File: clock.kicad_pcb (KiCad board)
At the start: 2 copper layers, 133 parts, among them J1 USB_C_Receptacle_USB2.0_16P, J3 Conn_01x02_Pin, J4 Conn_01x02_Pin, J5 Battery, Q1 2N7002K, Q2 NPN, SW1 SW_SPST, SW2 SW_SPST, SW5 SW_SPST, U1 STM32F072CBT6, U2 USBLC6-2SC6, U4 MCP73871-2CC, U5 AP2112K-3.3, Y1 8MHz

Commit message: am I ok??? is this too close. Nearly done!! mabye..
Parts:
- added C15: 10uF, Capacitor_SMD:C_0603_1608Metric_Pad1.08x0.95mm_HandSolder, F.Cu at (216.0, 38.5)
- added D1: D_Small, Diode_SMD:D_SOD-123F, F.Cu at (252.6, 59.6)
- added SW4: SW_SPDT, FB_clock_lib:SW_slide, B.Cu at (253.8, 44.0)
- D74, Q1, R12: moved to F.Cu
- moved BZ1 78.9 mm to (250.4, 58.8), turned to -90 degrees
- moved Q2 78.1 mm to (252.4, 51.0), turned to 0 degrees
- moved R13 75.5 mm to (249.8, 48.0), turned to -90 degrees
- moved Q1 61.1 mm to (227.3, 30.1)
- moved R12 60.9 mm to (230.8, 31.0), turned to 0 degrees
- moved R14 60.9 mm to (250.2, 42.0), turned to 90 degrees
- moved R15 59.9 mm to (249.0, 40.6), turned to -90 degrees
- moved R31 59.9 mm to (249.6, 44.9), turned to 90 degrees
- moved D74 58.9 mm to (248.1, 44.3), turned to 90 degrees
- moved R7 57.9 mm to (226.0, 33.6), turned to 180 degrees
- moved SW5 34.1 mm to (221.2, 61.6), turned to 0 degrees
- moved SW1 26.6 mm to (230.2, 61.6), turned to 0 degrees
- moved SW2 21.2 mm to (239.6, 61.6), turned to 0 degrees
- moved C7 1.61 mm to (252.6, 38.0), turned to 0 degrees
- moved C8 0.70 mm to (249.8, 37.4)
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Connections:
- U1 pad 10: unconnected-(U1-PA0-Pad10) -> 5V_TEST
- U1 pad 11: unconnected-(U1-PA1-Pad11) -> BUZZER
- U1 pad 39: LBO -> CE
- U1 pad 40: unconnected-(U1-PB4-Pad40) -> LBO
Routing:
- net GND: track 114.8 -> 156.4 mm, vias 15 -> 14
- net +5V: track 28.7 -> 65.9 mm, vias 4 -> 7
- net +3.3V: track 78.3 -> 107.2 mm, vias 2 -> 5
- net BUZZER: track 0.00 -> 13.8 mm
- net CE: track 0.00 -> 11.7 mm, vias 0 -> 1
- net 5V_TEST: track 0.00 -> 9.68 mm, vias 0 -> 2
- net Net-(BZ1--): track 0.00 -> 8.93 mm, vias 0 -> 1
- net Net-(Q1-D): track 0.00 -> 7.51 mm, vias 0 -> 1
- net Net-(SW4-B): track 0.00 -> 5.32 mm
- net M5: track 97.5 -> 94.9 mm
- net Net-(Q1-G): track 0.00 -> 2.00 mm
- net Net-(Q2-B): track 0.00 -> 1.89 mm
- net Net-(D74-A): track 0.00 -> 1.83 mm, vias 0 -> 1
- net LBO: track 33.4 -> 34.4 mm
- net M3: track 88.2 -> 87.4 mm
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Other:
- board outline added: 51.4 x 38.8 mm

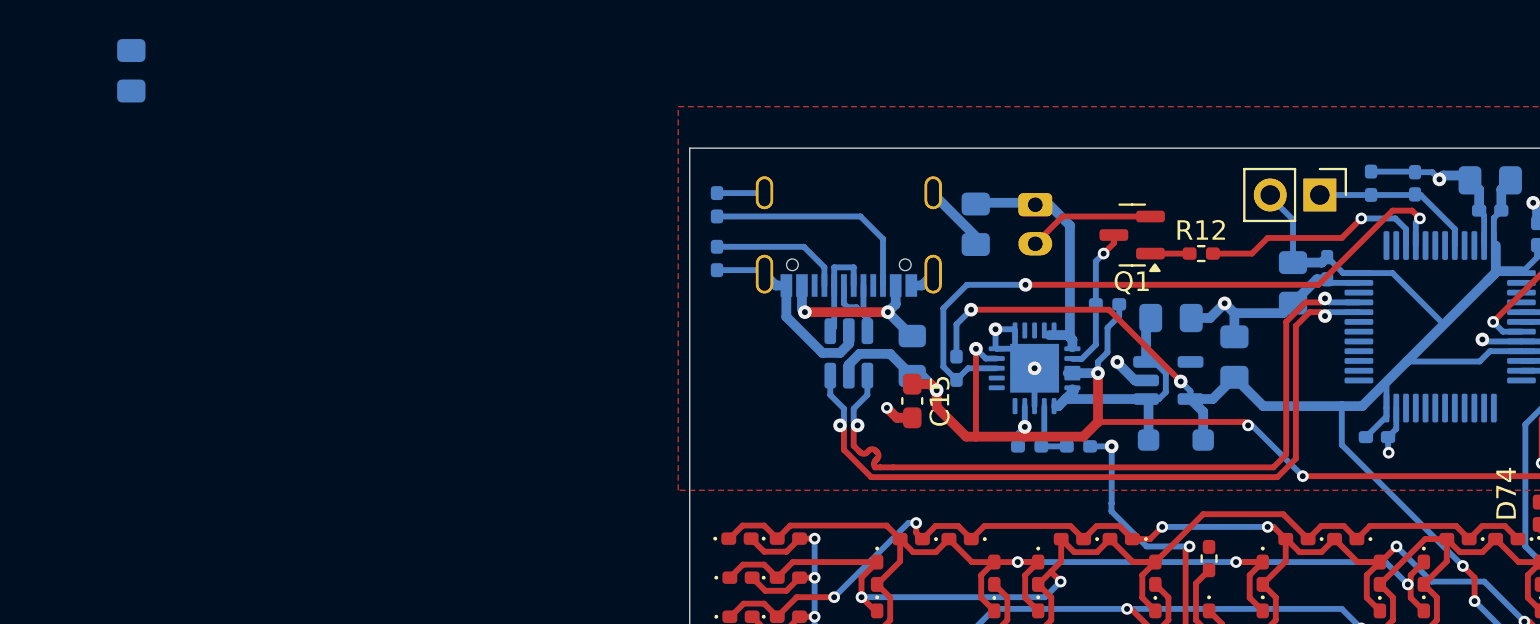
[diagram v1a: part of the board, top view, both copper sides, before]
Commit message: fixed weird kicad bug, added last few components, just need to add charlie plexed resistors + wire it up
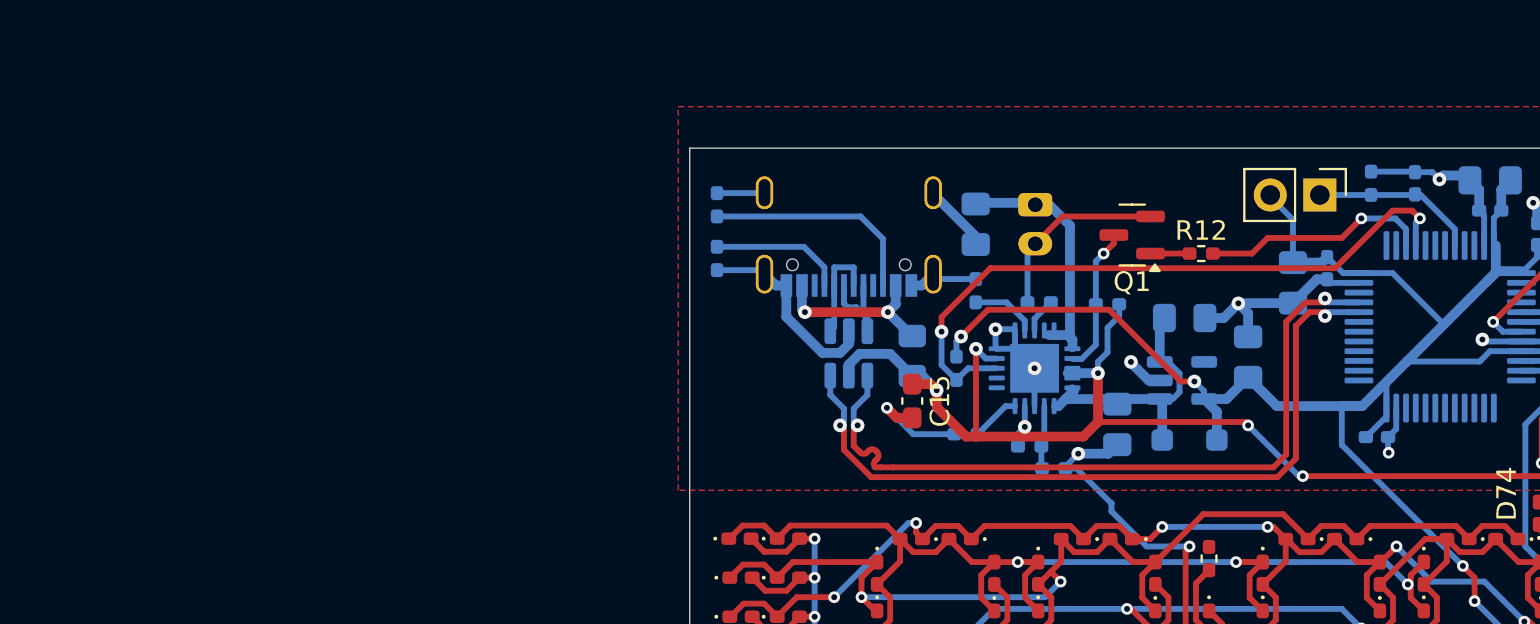
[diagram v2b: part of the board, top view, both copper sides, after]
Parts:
- added R5: 2k, Resistor_SMD:R_0402_1005Metric_Pad0.72x0.64mm_HandSolder, B.Cu at (222.5, 33.5)
- added R8: 100k, Resistor_SMD:R_0402_1005Metric_Pad0.72x0.64mm_HandSolder, B.Cu at (219.2, 32.9)
- added R9: 10k, Resistor_SMD:R_0402_1005Metric_Pad0.72x0.64mm_HandSolder, B.Cu at (218.8, 40.2)
- moved C16 53.6 mm to (226.5, 39.8), turned to 90 degrees
- moved R11 1.69 mm to (223.2, 42.0)
- moved C18 0.70 mm to (229.9, 34.3)
- moved C19 0.70 mm to (233.2, 36.3)
- moved D76 0.70 mm to (230.2, 40.5)
- moved U5 0.70 mm to (229.8, 37.5)
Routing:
- net GND: track 156.4 -> 167.9 mm
- net Net-(U4-PROG3): track 0.00 -> 3.40 mm
- net Net-(U4-THERM): track 0.00 -> 2.51 mm
- net Net-(U4-PROG1): track 0.00 -> 1.78 mm
- net VCC: track 13.3 -> 14.0 mm

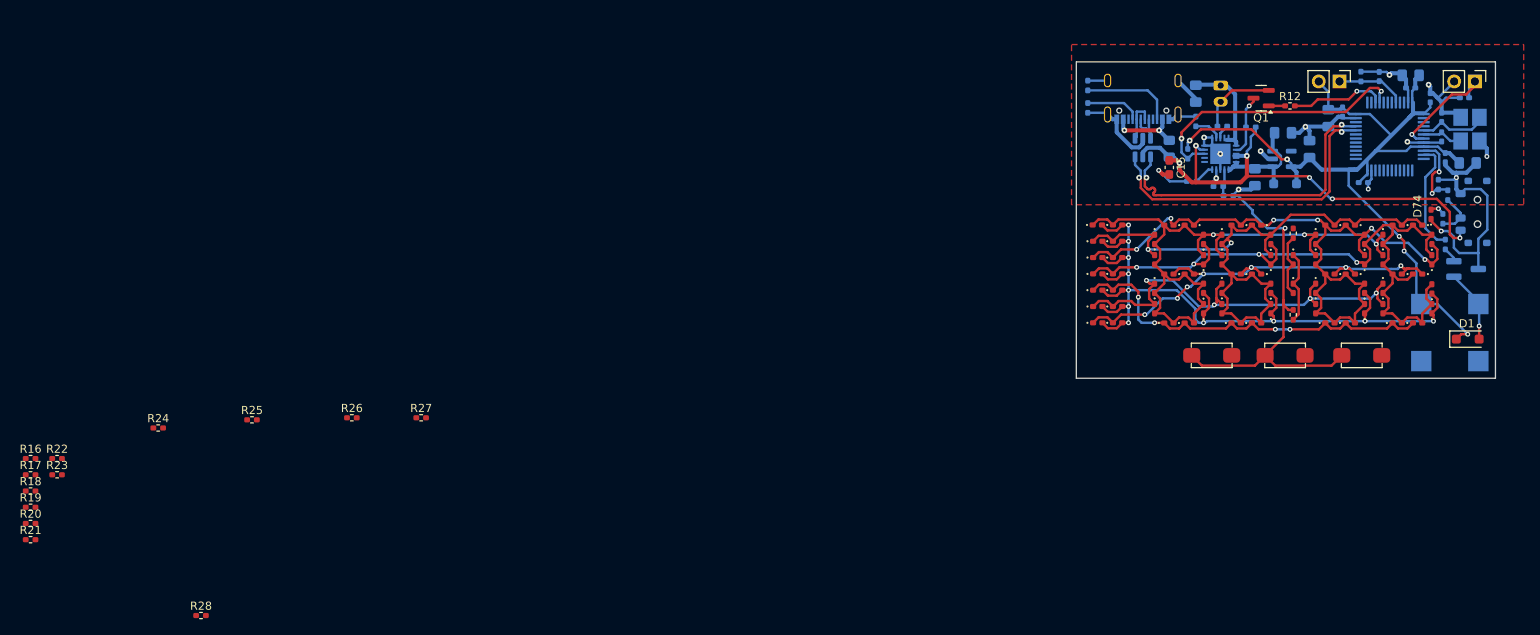
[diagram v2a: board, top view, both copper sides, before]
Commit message: all wiring done, need to clean up silk screen edge clips + double check pins for charlieplex & buttons
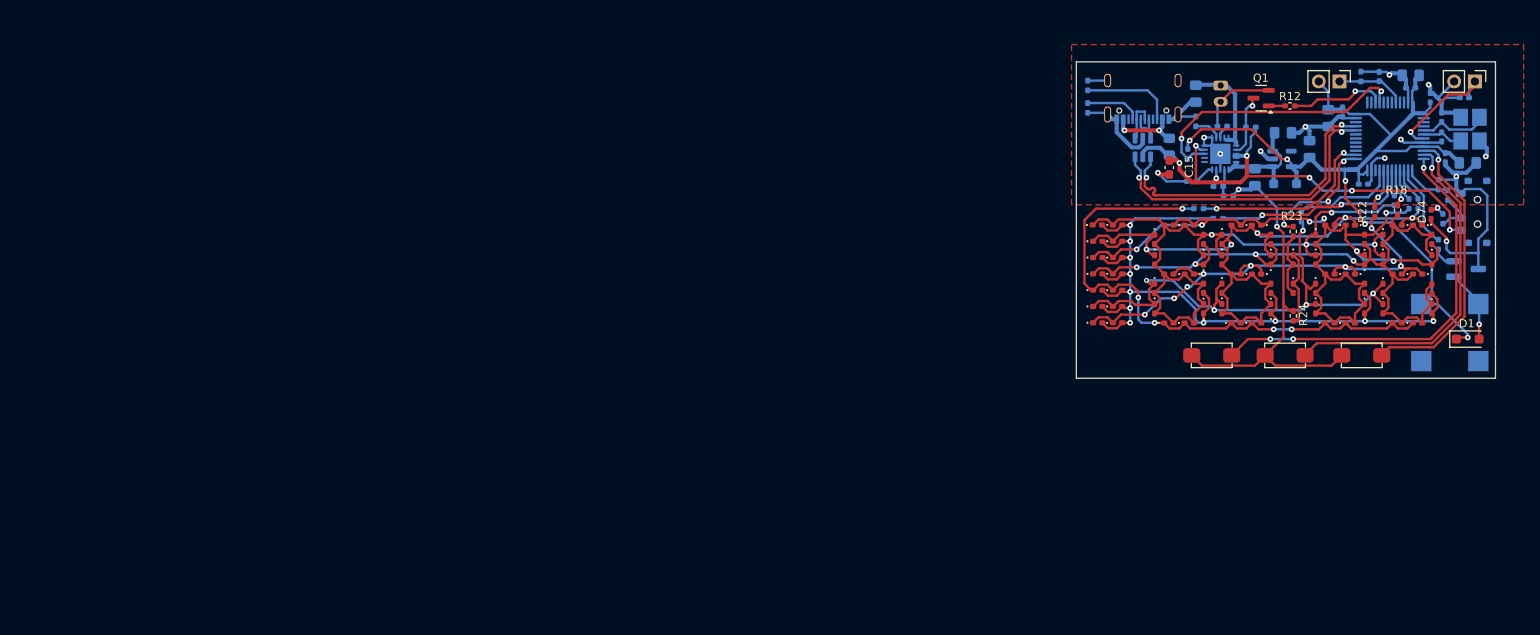
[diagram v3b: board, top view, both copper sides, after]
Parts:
- removed R25, R26, R27, R28, R29, R30: 68R, Resistor_SMD:R_0402_1005Metric_Pad0.72x0.64mm_HandSolder
- added R3: 50R, Resistor_SMD:R_0402_1005Metric_Pad0.72x0.64mm_HandSolder, B.Cu at (246.5, 43.0)
- R16, R17, R19, R20, R21: value 68R -> 50R; moved to B.Cu
- R18, R22, R23, R24: value 68R -> 50R
- moved R17 172.3 mm to (245.4, 43.0), turned to -90 degrees
- moved R18 171.2 mm to (244.0, 43.8), turned to -90 degrees
- moved R16 170.2 mm to (243.6, 42.6), turned to -90 degrees
- moved R22 164.4 mm to (241.2, 44.0), turned to -90 degrees
- moved R21 160.8 mm to (232.2, 44.6), turned to -90 degrees
- moved R23 154.5 mm to (231.2, 46.4), turned to 90 degrees
- moved R19 149.9 mm to (222.0, 44.8), turned to 180 degrees
- moved R20 148.4 mm to (219.6, 43.6), turned to 180 degrees
- moved R24 139.9 mm to (231.2, 56.8), turned to -90 degrees
- moved R13 0.85 mm to (249.0, 48.0)
- moved F1 0.25 mm to (216.0, 36.0)
- moved C4 0.20 mm to (239.8, 40.6)
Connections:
- D10 pad 1: M3 -> /LED's/R3
- D10 pad 2: M1 -> /LED's/R1
- D11 pad 1: M4 -> /LED's/R4
- D11 pad 2: M1 -> /LED's/R1
- D12 pad 1: M5 -> /LED's/R5
- D12 pad 2: M1 -> /LED's/R1
- D13 pad 1: M6 -> /LED's/R6
- D13 pad 2: M1 -> /LED's/R1
- D14 pad 1: M7 -> /LED's/R7
- D14 pad 2: M1 -> /LED's/R1
- D15 pad 1: M8 -> /LED's/R8
- D15 pad 2: M1 -> /LED's/R1
- D16 pad 1: M1 -> /LED's/R1
- D16 pad 2: M2 -> /LED's/R2
- D17 pad 1: M3 -> /LED's/R3
- D17 pad 2: M2 -> /LED's/R2
- D18 pad 1: M4 -> /LED's/R4
- D18 pad 2: M2 -> /LED's/R2
- D19 pad 1: M5 -> /LED's/R5
- D19 pad 2: M2 -> /LED's/R2
- D2 pad 1: M2 -> /LED's/R2
- D2 pad 2: M1 -> /LED's/R1
- D20 pad 1: M6 -> /LED's/R6
- D20 pad 2: M2 -> /LED's/R2
- D21 pad 1: M7 -> /LED's/R7
- D21 pad 2: M2 -> /LED's/R2
- D22 pad 1: M8 -> /LED's/R8
- D22 pad 2: M2 -> /LED's/R2
- D23 pad 1: M1 -> /LED's/R1
- D23 pad 2: M2 -> /LED's/R2
- D24 pad 1: M3 -> /LED's/R3
- D24 pad 2: M2 -> /LED's/R2
- D25 pad 1: M4 -> /LED's/R4
- D25 pad 2: M2 -> /LED's/R2
- D26 pad 1: M5 -> /LED's/R5
- D26 pad 2: M2 -> /LED's/R2
- D27 pad 1: M6 -> /LED's/R6
- D27 pad 2: M2 -> /LED's/R2
- D28 pad 1: M7 -> /LED's/R7
- D28 pad 2: M2 -> /LED's/R2
- D29 pad 1: M8 -> /LED's/R8
- D29 pad 2: M2 -> /LED's/R2
- D3 pad 1: M3 -> /LED's/R3
- D3 pad 2: M1 -> /LED's/R1
- D30 pad 1: M1 -> /LED's/R1
- D30 pad 2: M3 -> /LED's/R3
- D31 pad 1: M2 -> /LED's/R2
- D31 pad 2: M3 -> /LED's/R3
- D32 pad 1: M4 -> /LED's/R4
- D32 pad 2: M3 -> /LED's/R3
- D33 pad 1: M5 -> /LED's/R5
- D33 pad 2: M3 -> /LED's/R3
- D34 pad 1: M6 -> /LED's/R6
- D34 pad 2: M3 -> /LED's/R3
- D35 pad 1: M7 -> /LED's/R7
- D35 pad 2: M3 -> /LED's/R3
- D36 pad 1: M8 -> /LED's/R8
- D36 pad 2: M3 -> /LED's/R3
- D37 pad 1: M1 -> /LED's/R1
- D37 pad 2: M3 -> /LED's/R3
- D38 pad 1: M2 -> /LED's/R2
- D38 pad 2: M3 -> /LED's/R3
- D39 pad 1: M4 -> /LED's/R4
- D39 pad 2: M3 -> /LED's/R3
- D4 pad 1: M4 -> /LED's/R4
- D4 pad 2: M1 -> /LED's/R1
- D40 pad 1: M5 -> /LED's/R5
- D40 pad 2: M3 -> /LED's/R3
- D41 pad 1: M6 -> /LED's/R6
- D41 pad 2: M3 -> /LED's/R3
- D42 pad 1: M7 -> /LED's/R7
- D42 pad 2: M3 -> /LED's/R3
- D43 pad 1: M8 -> /LED's/R8
- D43 pad 2: M3 -> /LED's/R3
- D44 pad 1: M1 -> /LED's/R1
- D44 pad 2: M4 -> /LED's/R4
- D45 pad 1: M2 -> /LED's/R2
- D45 pad 2: M4 -> /LED's/R4
- D46 pad 1: M3 -> /LED's/R3
- D46 pad 2: M4 -> /LED's/R4
- D47 pad 1: M5 -> /LED's/R5
- D47 pad 2: M4 -> /LED's/R4
- D48 pad 1: M6 -> /LED's/R6
- D48 pad 2: M4 -> /LED's/R4
- D49 pad 1: M7 -> /LED's/R7
- D49 pad 2: M4 -> /LED's/R4
- D5 pad 1: M5 -> /LED's/R5
- D5 pad 2: M1 -> /LED's/R1
- D50 pad 1: M8 -> /LED's/R8
- D50 pad 2: M4 -> /LED's/R4
- D51 pad 1: M1 -> /LED's/R1
- D51 pad 2: M4 -> /LED's/R4
- D52 pad 1: M2 -> /LED's/R2
- D52 pad 2: M4 -> /LED's/R4
- D53 pad 1: M3 -> /LED's/R3
- D53 pad 2: M4 -> /LED's/R4
- D54 pad 1: M5 -> /LED's/R5
- D54 pad 2: M4 -> /LED's/R4
- D55 pad 1: M6 -> /LED's/R6
- D55 pad 2: M4 -> /LED's/R4
- D56 pad 1: M7 -> /LED's/R7
- D56 pad 2: M4 -> /LED's/R4
- D57 pad 1: M8 -> /LED's/R8
- D57 pad 2: M4 -> /LED's/R4
- D58 pad 1: M1 -> /LED's/R1
- D58 pad 2: M5 -> /LED's/R5
- D59 pad 1: M2 -> /LED's/R2
- D59 pad 2: M5 -> /LED's/R5
- D6 pad 1: M6 -> /LED's/R6
- D6 pad 2: M1 -> /LED's/R1
- D60 pad 1: M3 -> /LED's/R3
- D60 pad 2: M5 -> /LED's/R5
- D61 pad 1: M4 -> /LED's/R4
- D61 pad 2: M5 -> /LED's/R5
- D62 pad 1: M6 -> /LED's/R6
- D62 pad 2: M5 -> /LED's/R5
- D63 pad 1: M7 -> /LED's/R7
- D63 pad 2: M5 -> /LED's/R5
- D64 pad 1: M8 -> /LED's/R8
- D64 pad 2: M5 -> /LED's/R5
- D65 pad 1: M1 -> /LED's/R1
- D65 pad 2: M5 -> /LED's/R5
- D66 pad 1: M2 -> /LED's/R2
- D66 pad 2: M5 -> /LED's/R5
- D67 pad 1: M3 -> /LED's/R3
- D67 pad 2: M5 -> /LED's/R5
- D68 pad 1: M4 -> /LED's/R4
- D68 pad 2: M5 -> /LED's/R5
- D69 pad 1: M6 -> /LED's/R6
- D69 pad 2: M5 -> /LED's/R5
- D7 pad 1: M7 -> /LED's/R7
- D7 pad 2: M1 -> /LED's/R1
- D70 pad 1: M7 -> /LED's/R7
- D70 pad 2: M5 -> /LED's/R5
- D71 pad 1: M8 -> /LED's/R8
- D71 pad 2: M5 -> /LED's/R5
- D8 pad 1: M8 -> /LED's/R8
- D8 pad 2: M1 -> /LED's/R1
- D9 pad 1: M2 -> /LED's/R2
- D9 pad 2: M1 -> /LED's/R1
- R16 pad 2: M1 -> /LED's/R1
- R17 pad 1: M2 -> M3
- R17 pad 2: M2 -> /LED's/R3
- R18 pad 1: M3 -> M4
- R18 pad 2: M3 -> /LED's/R4
- R19 pad 1: M4 -> M5
- R19 pad 2: M4 -> /LED's/R5
- R20 pad 1: M5 -> M6
- R20 pad 2: M5 -> /LED's/R6
- R21 pad 1: M6 -> M7
- R21 pad 2: M6 -> /LED's/R7
- R22 pad 1: M7 -> M8
- R22 pad 2: M7 -> /LED's/R8
- R23 pad 1: M8 -> Net-(D72-A)
- R23 pad 2: M8 -> COLON
- R24 pad 1: M1 -> GND
- R24 pad 2: M1 -> Net-(D72-K)
- U1 pad 10: 5V_TEST -> RIGHT
- U1 pad 11: BUZZER -> SELECT
- U1 pad 12: unconnected-(U1-PA2-Pad12) -> LEFT
- U1 pad 13: unconnected-(U1-PA3-Pad13) -> 5V_TEST
- U1 pad 14: unconnected-(U1-PA4-Pad14) -> BUZZER
- U1 pad 15: unconnected-(U1-PA5-Pad15) -> M2
- U1 pad 16: unconnected-(U1-PA6-Pad16) -> M3
- U1 pad 17: unconnected-(U1-PA7-Pad17) -> M4
- U1 pad 18: unconnected-(U1-PB0-Pad18) -> M1
- U1 pad 19: unconnected-(U1-PB1-Pad19) -> M5
- U1 pad 20: unconnected-(U1-PB2-Pad20) -> M8
- U1 pad 21: unconnected-(U1-PB10-Pad21) -> M7
- U1 pad 25: unconnected-(U1-PB12-Pad25) -> COLON
- U1 pad 26: unconnected-(U1-PB13-Pad26) -> M6
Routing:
- net /LED's/R5: track 0.00 -> 106.9 mm, vias 0 -> 11
- net /LED's/R3: track 0.00 -> 100.4 mm, vias 0 -> 7
- net /LED's/R1: track 0.00 -> 96.1 mm, vias 0 -> 4
- net /LED's/R2: track 0.00 -> 92.9 mm, vias 0 -> 5
- net /LED's/R4: track 0.00 -> 88.3 mm, vias 0 -> 4
- net M4: track 89.1 -> 4.74 mm, vias 4 -> 1
- net M3: track 87.4 -> 3.95 mm, vias 6 -> 0
- net M2: track 84.7 -> 4.20 mm, vias 2 -> 0
- net M1: track 83.0 -> 3.22 mm, vias 3 -> 0
- net /LED's/R6: track 0.00 -> 71.1 mm, vias 0 -> 5
- net M5: track 94.9 -> 24.4 mm, vias 11 -> 2
- net /LED's/R8: track 0.00 -> 65.4 mm, vias 0 -> 8
- net /LED's/R7: track 0.00 -> 64.7 mm, vias 0 -> 5
- net M8: track 56.0 -> 4.94 mm, vias 7 -> 1
- net LEFT: track 0.00 -> 50.3 mm, vias 0 -> 3
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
